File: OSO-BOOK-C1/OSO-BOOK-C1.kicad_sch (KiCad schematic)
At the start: 31 parts, among them J1 JST-PH3, J2 JST-PH3, J3 JST-PH4, Q1 Q_PMOS_GSD, Q2 Q_PMOS_GSD, SW1 SW_SPDT, U1 Pico, U2 OSO-BOOK-C2-01, U3 MEM2075, U4 GD25Q16C

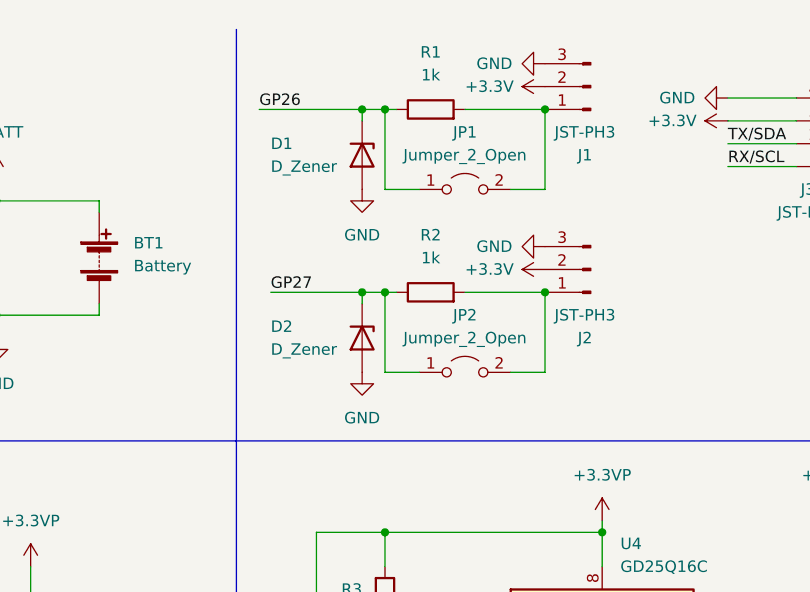
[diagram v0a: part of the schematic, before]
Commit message: rev 5: remove zener diodes, silkscreen tweaks
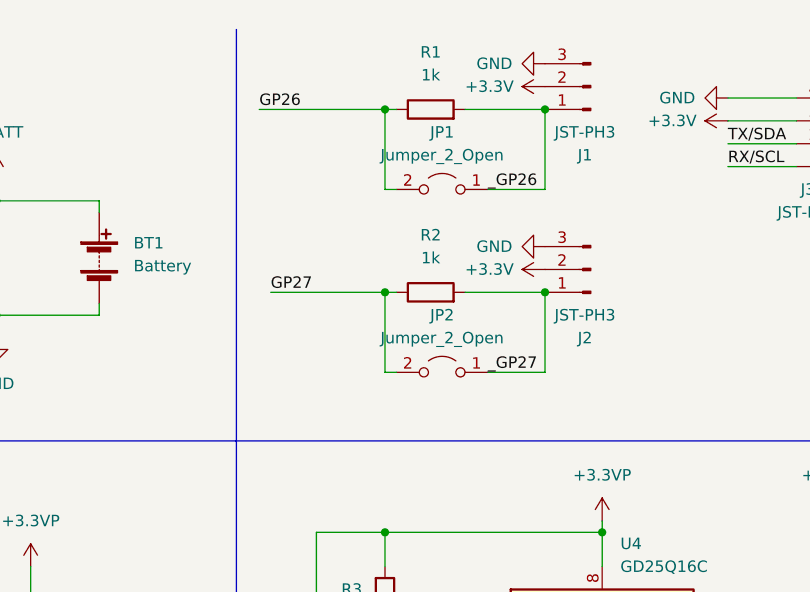
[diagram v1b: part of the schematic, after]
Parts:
- removed D1, D2: D_Zener, Diode_SMD:D_SOD-123F, symbol Device:D_Zener
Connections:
- net GP26: now also JP1.2 (B); no longer JP1.1 (A)
- net GP27: now also JP2.2 (B); no longer JP2.1 (A)
- net _GP27: now reaches J2.1 (Pin_1), R2.2
- net _GP27: now also JP2.1 (A); no longer JP2.2 (B)
- net _GP26: now reaches J1.1 (Pin_1), R1.2
- net _GP26: now also JP1.1 (A); no longer JP1.2 (B)
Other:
- moved on the sheet: JP1, JP2
